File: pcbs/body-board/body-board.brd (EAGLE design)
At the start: 43 x 72.5 mm, 29 parts, among them X1 2520-

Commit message: Update boards to latest
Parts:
- J1, J10, J2, J3, J4, J5, J6, J7, J8, J9: device SparkFun-Connectors:JST-2-PTH -> SparkFun-Connectors:1X02_2.54_SCREWTERM
- moved J1 3.61 mm to (5.00, 60.0), turned to 270 degrees
- moved J8 3.61 mm to (39.0, 30.0), turned to 90 degrees
- moved J10 2.83 mm to (39.0, 20.0), turned to 90 degrees
- moved J2 2.83 mm to (5.00, 51.0), turned to 270 degrees
- moved J7 2.83 mm to (39.0, 39.0), turned to 90 degrees
- moved J3 2.24 mm to (5.00, 42.0), turned to 270 degrees
- moved J6 2.24 mm to (39.0, 48.0), turned to 90 degrees
- moved J4 2.00 mm to (5.00, 33.0), turned to 270 degrees
- moved J5 2.00 mm to (39.0, 57.0), turned to 90 degrees
- moved J9 2.00 mm to (5.00, 22.0), turned to 270 degrees
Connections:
- net N$10: now also J7.P2; no longer J7.2
- net N$11: now also J6.P2; no longer J6.2
- net N$12: now also J5.P2; no longer J5.2
- net N$13: now also J1.P2; no longer J1.2
- net N$14: now also J2.P2; no longer J2.2
- net N$15: now also J3.P2; no longer J3.2
- net N$16: now also J4.P2; no longer J4.2
- net N$8: now also J10.P2, J9.P2; no longer J10.2, J9.2
- net N$9: now also J8.P2; no longer J8.2
- net VIN: now also J1.P1, J10.P1, J2.P1, J3.P1, J4.P1, J5.P1, J6.P1, J7.P1, J8.P1, J9.P1; no longer J1.1, J10.1, J2.1, J3.1, J4.1, J5.1, J6.1, J7.1, J8.1, J9.1
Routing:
- net N$13: track 55.1 -> 63.5 mm
- net N$12: track 59.1 -> 66.1 mm
- net N$14: track 46.0 -> 51.4 mm
- net N$15: track 36.9 -> 41.0 mm
- net N$11: track 50.1 -> 54.1 mm
- net N$16: track 27.9 -> 31.6 mm
- net N$10: track 41.0 -> 44.4 mm
- net N$9: track 31.4 -> 33.6 mm
- net N$8: track 48.0 -> 50.3 mm

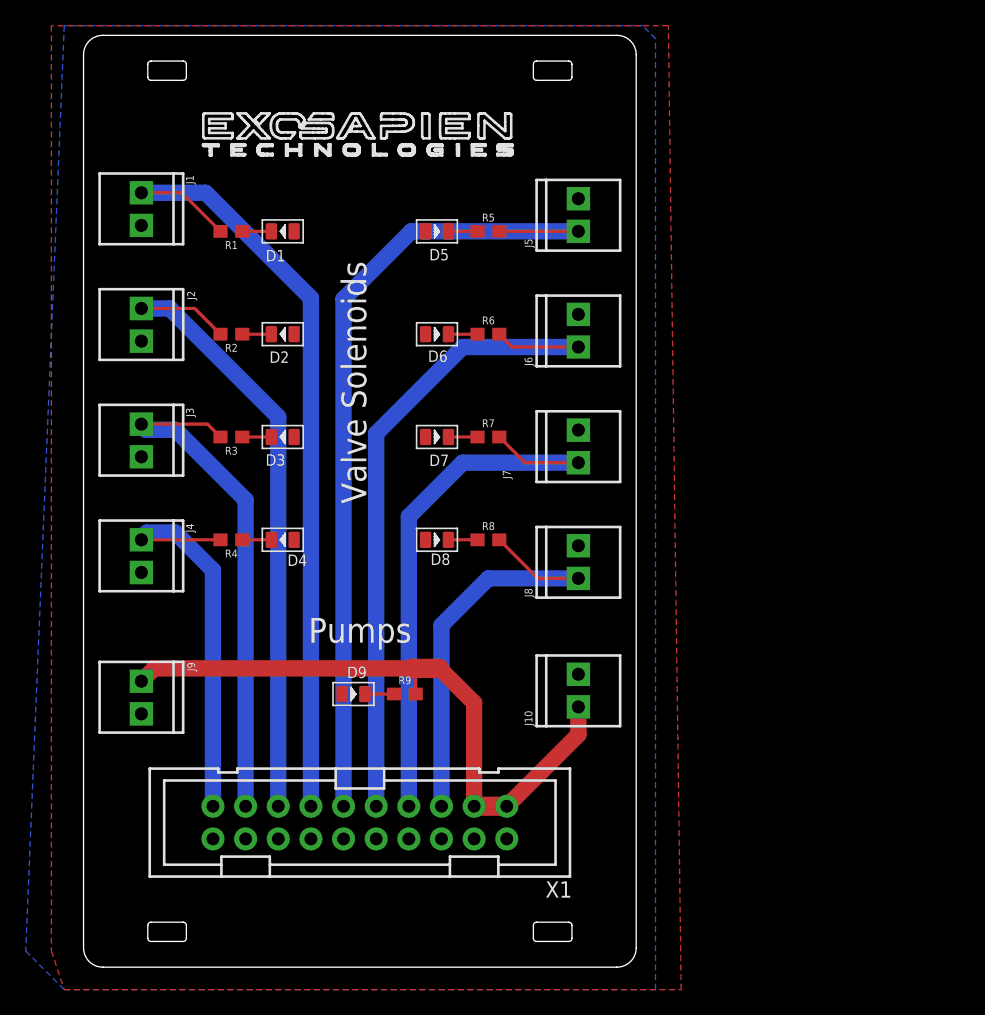
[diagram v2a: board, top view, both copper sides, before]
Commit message: Updated body board sans creation crate logo
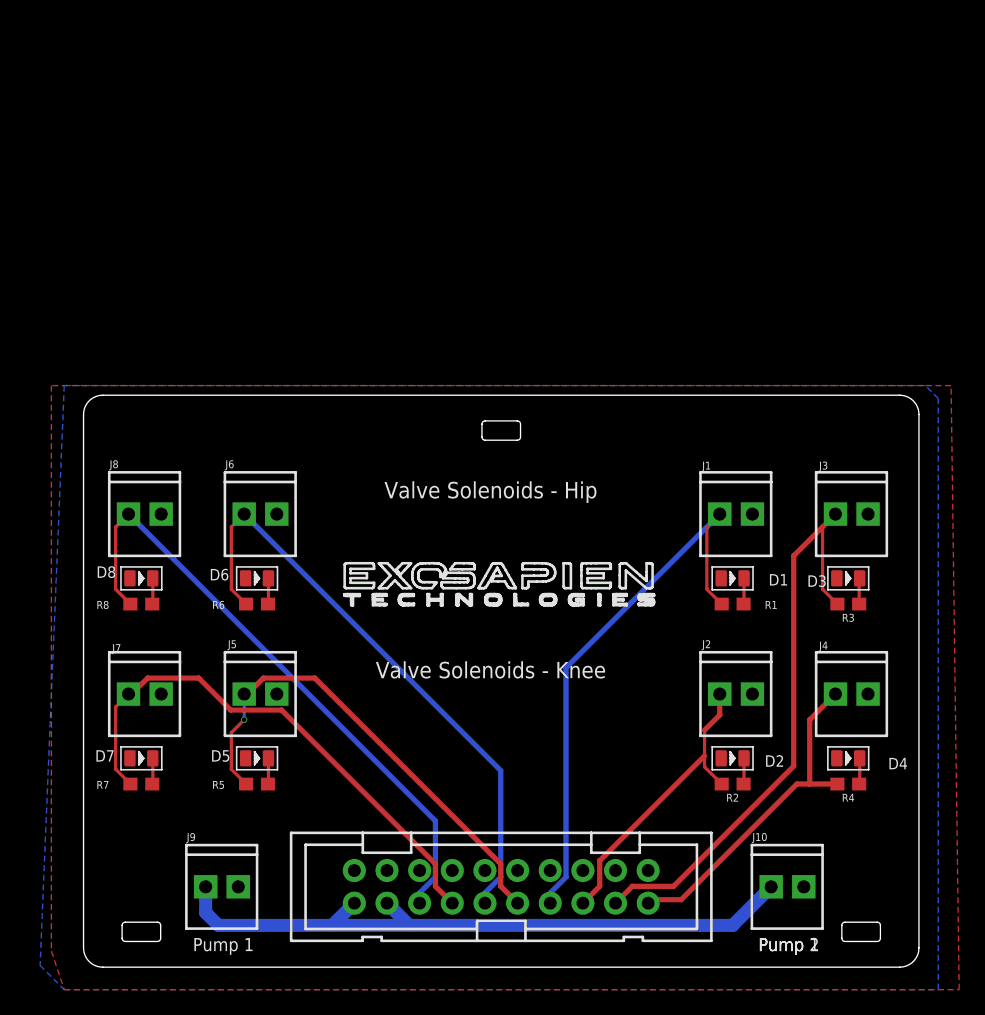
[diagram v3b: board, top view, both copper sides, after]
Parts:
- removed D9: RED-0805, OPL_Optoelectronics:LED-0805
- removed R9: 1k, SparkFun-Resistors:0603
- moved J4 55.3 mm to (59.0, 21.0), turned to 0 degrees
- moved J3 54.5 mm to (59.0, 35.0), turned to 0 degrees
- moved J2 54.1 mm to (50.0, 21.0), turned to 0 degrees
- moved R2 52.4 mm to (51.0, 14.0)
- moved R4 51.6 mm to (60.0, 14.0)
- moved J1 51.5 mm to (50.0, 35.0), turned to 0 degrees
- moved R3 49.7 mm to (60.0, 28.0)
- moved R1 48.6 mm to (51.0, 28.0)
- moved D2 48.1 mm to (51.0, 16.0), turned to 0 degrees
- moved D4 47.2 mm to (60.0, 16.0), turned to 0 degrees
- moved R5 46.6 mm to (14.0, 14.0), turned to 180 degrees
- moved D3 45.4 mm to (60.0, 30.0), turned to 0 degrees
- moved J5 44.4 mm to (13.0, 21.0), turned to 0 degrees
- moved D1 44.2 mm to (51.0, 30.0), turned to 0 degrees
- moved D5 43.3 mm to (14.0, 16.0)
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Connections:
- removed net N$7: D9.-, R9.1
- net N$8: no longer R9.2
- net VIN: no longer D9.+
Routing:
- net N$12: track 66.1 -> 38.0 mm, vias 0 -> 1
- net N$14: track 51.4 -> 23.4 mm
- net N$13: track 63.5 -> 43.6 mm
- net N$9: track 33.6 -> 48.6 mm
- net N$11: track 54.1 -> 46.9 mm
- net N$15: track 41.0 -> 47.1 mm
- net N$16: track 31.6 -> 26.4 mm
- net N$10: track 44.4 -> 41.9 mm
- net N$8: track 50.3 -> 52.6 mm
- net N$7: track 2.26 -> 0.00 mm
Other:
- board size 43 x 72.5 mm -> 65 x 44.5 mm
- board text added: "Pump 1"
- board text added: "Pump 2"
- board text added: "Valve Solenoids - Hip"
- board text added: "Valve Solenoids - Knee"
- board text removed: "Pumps"
- board text removed: "Valve Solenoids"
